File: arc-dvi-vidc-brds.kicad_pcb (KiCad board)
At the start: 4 copper layers, 75.8 x 90.5 mm, 32 parts, among them IC1 SN74ALVC164245, IC2 SN74ALVC164245, IC3 SN74ALVC164245, J1 Connector_50pin_FFC, U1 MIC5219 3.3V

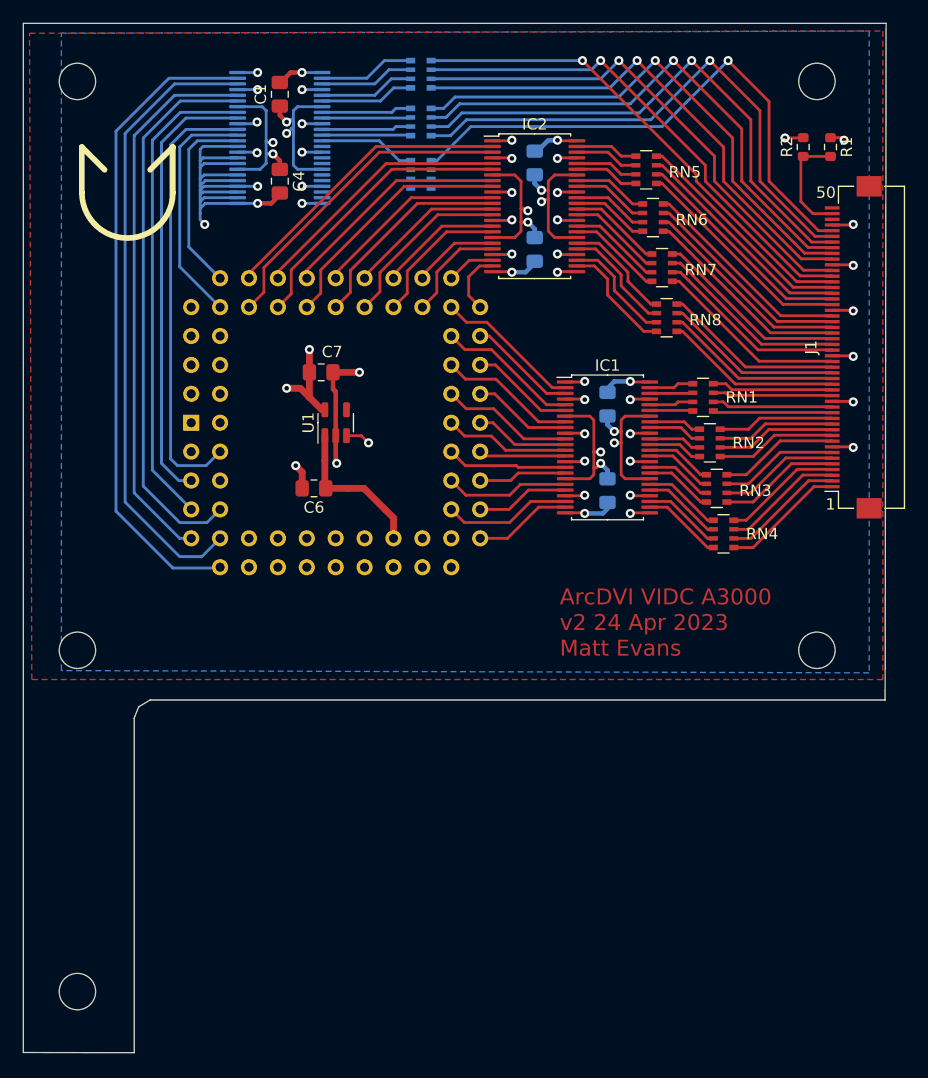
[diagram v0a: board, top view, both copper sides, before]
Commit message: Tweaks to cap positions, power planes
In good shape now, a few minor tweaks to go
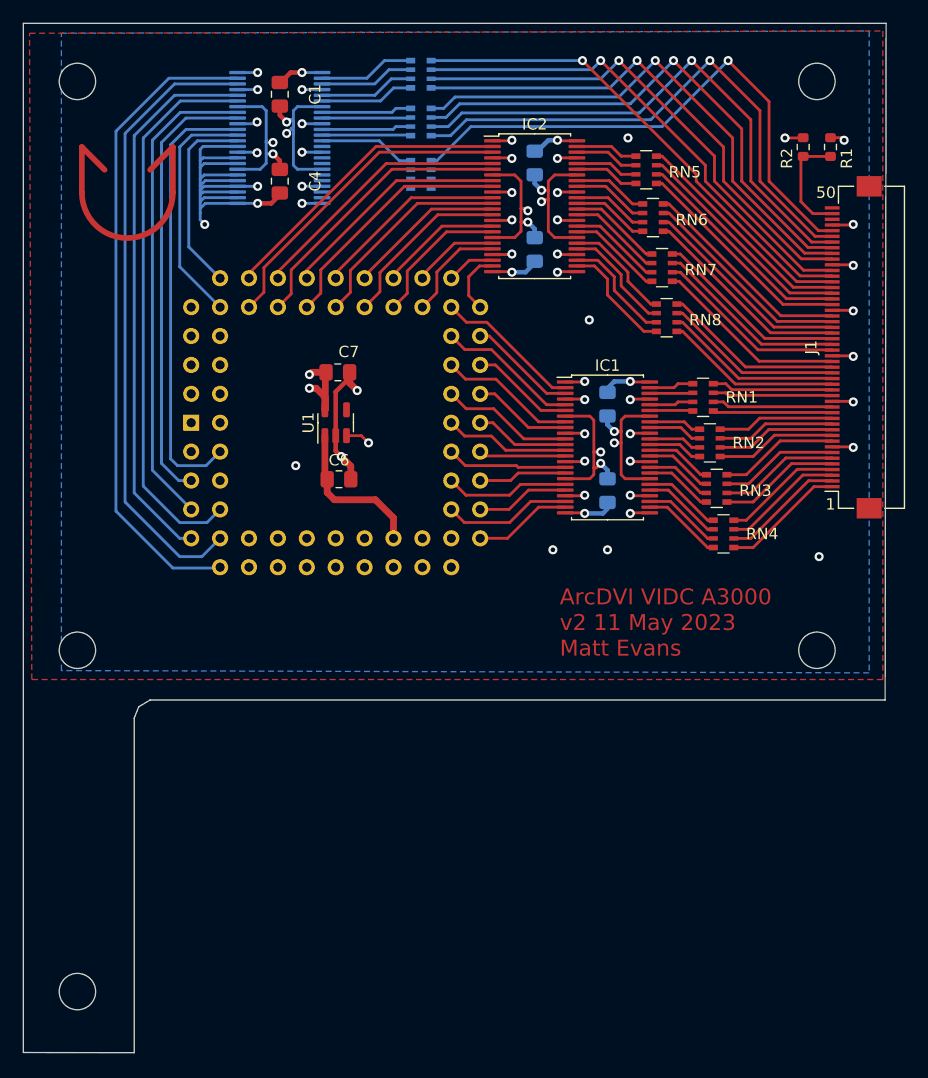
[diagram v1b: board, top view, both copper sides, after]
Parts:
- moved C6 2.34 mm to (83.0, 105.0), turned to 0 degrees
- moved C7 1.46 mm to (82.9, 95.6)
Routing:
- net +3V3: track 242.3 -> 240.2 mm
- net GND: track 413.6 -> 413.3 mm, vias 47 -> 52
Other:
- board text added: "ArcDVI VIDC A3000 v2 11 May 2023 Matt Evans"
- board text removed: "ArcDVI VIDC A3000 v2 24 Apr 2023 Matt Evans"

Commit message: Add logo
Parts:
- added G***: LOGO, LOGO, F.Cu at (94.5, 71.7)

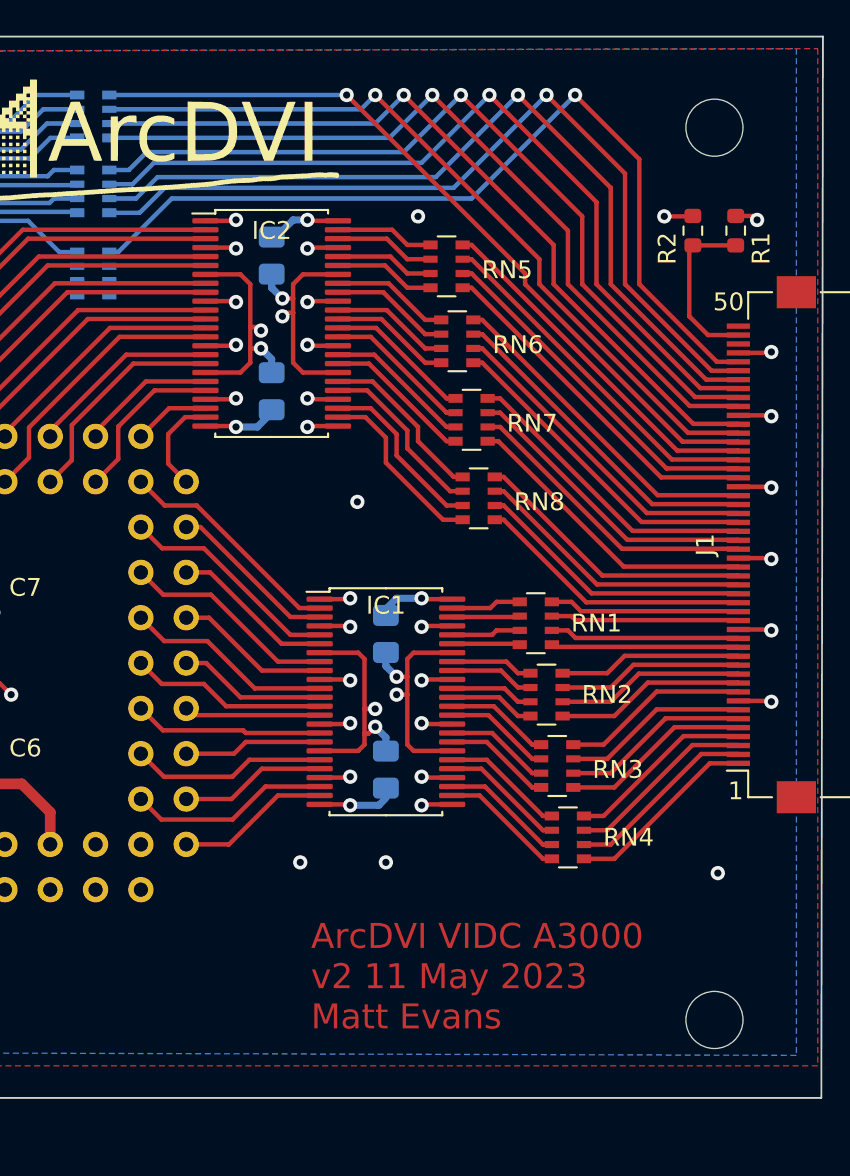
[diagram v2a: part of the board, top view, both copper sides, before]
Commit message: Moved holes to 60mm centers
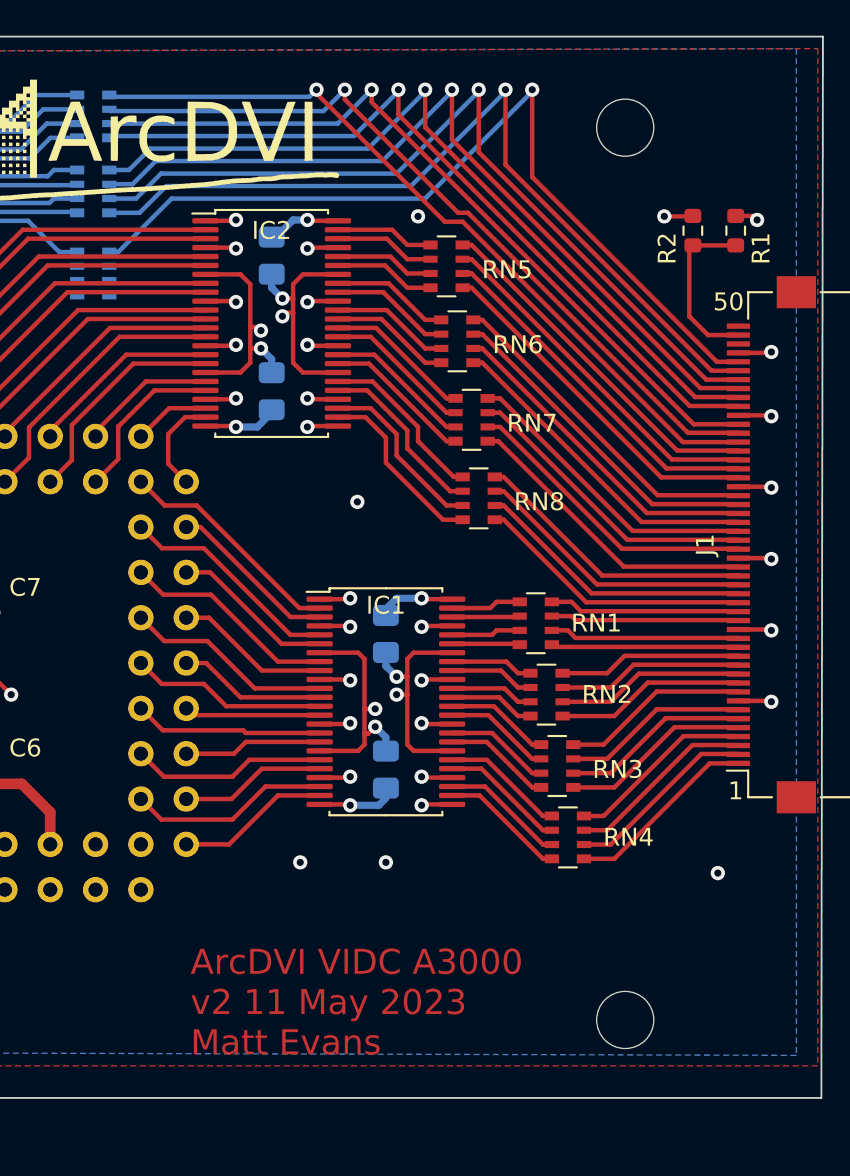
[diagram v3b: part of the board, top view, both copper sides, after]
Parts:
- moved REF** 5.00 mm to (120.0, 120.0)
- moved REF** 5.00 mm to (120.0, 70.0)
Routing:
- net Net-(J1-Pad46): track 49.2 -> 48.3 mm
- net Net-(J1-Pad45): track 48.0 -> 47.2 mm
- net Net-(J1-Pad44): track 47.4 -> 46.6 mm
- net Net-(J1-Pad43): track 46.8 -> 46.1 mm
- net Net-(J1-Pad42): track 46.2 -> 45.5 mm
- net Net-(J1-Pad39): track 44.8 -> 44.2 mm
- net Net-(J1-Pad41): track 45.2 -> 44.6 mm

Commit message: Update date
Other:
- board text added: "ArcDVI VIDC A3000 v2 1 June 2023 Matt Evans"
- board text removed: "ArcDVI VIDC A3000 v2 11 May 2023 Matt Evans"
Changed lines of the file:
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@@
       (xy 131.08 64.895)
     ) (layer "Edge.Cuts") (width 0.1) (fill none))
-  (gr_text "ArcDVI VIDC A3000\nv2 11 May 2023\nMatt Evans" (at 95.64 119.02) (layer "F.Cu")
+  (gr_text "ArcDVI VIDC A3000\nv2 1 June 2023\nMatt Evans" (at 95.64 119.02) (layer "F.Cu")
     (effects (font (size 1.4 1.4) (thickness 0.25)) (justify left))
   )

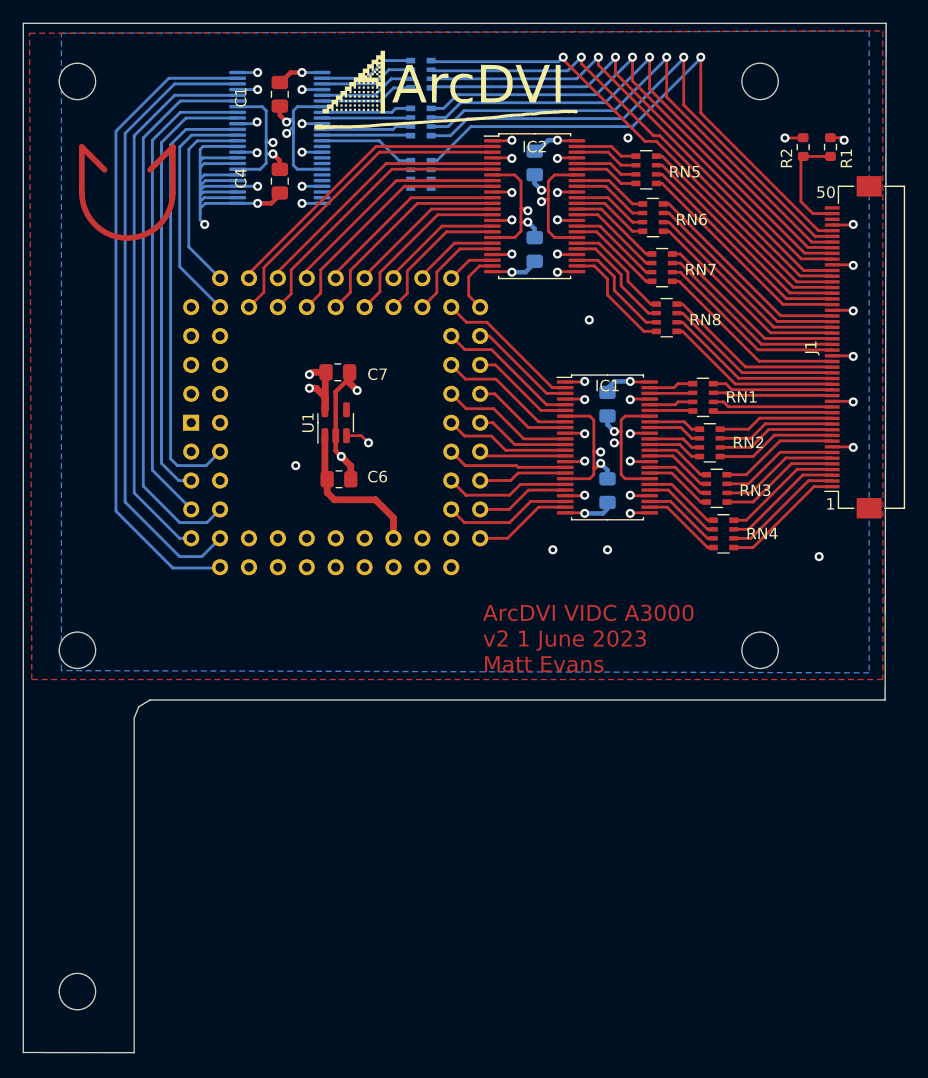
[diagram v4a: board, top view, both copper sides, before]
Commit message: Move regulator, move holes
Reg move now makes PLCC socket centre bare, ideal for mechanical pressure point.
Holes now mean main ArcDVI board lines up preciselyish.
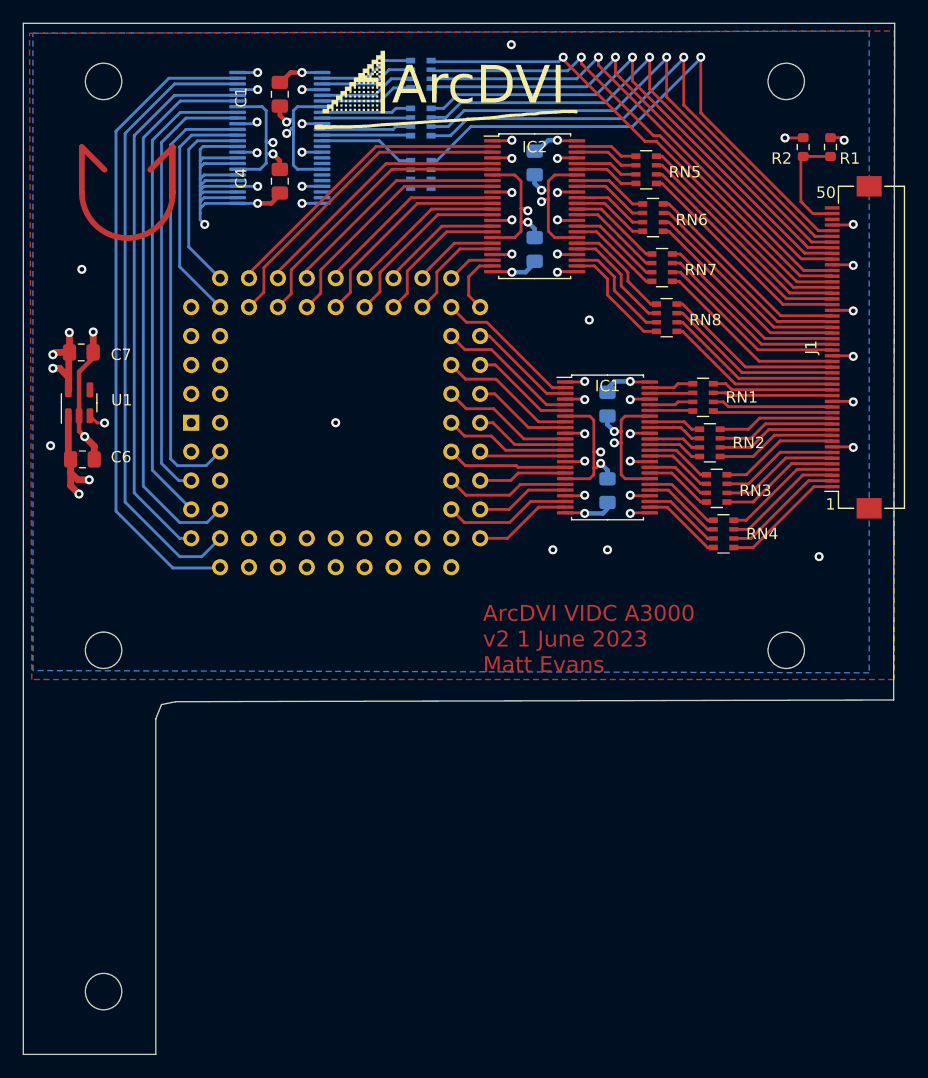
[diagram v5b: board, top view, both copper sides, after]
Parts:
- moved U1 22.6 mm to (60.1, 98.2)
- moved C6 22.6 mm to (60.4, 103.2)
- moved C7 22.6 mm to (60.3, 93.8)
- moved REF** 2.30 mm to (122.3, 120.0)
- moved REF** 2.30 mm to (62.3, 150.0)
- moved REF** 2.30 mm to (122.3, 70.0)
- moved REF** 2.30 mm to (62.3, 120.0)
- moved REF** 2.30 mm to (62.3, 70.0)
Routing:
- net +3V3: track 240.2 -> 179.7 mm, vias 9 -> 10
- net +5V: track 170.7 -> 208.7 mm, vias 7 -> 9
- net GND: track 413.3 -> 408.2 mm, vias 52 -> 54
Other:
- board size 75.8 x 90.5 mm -> 76.6 x 90.6 mm
- board text added: "From TR hole, 20.4 across, 30 down"

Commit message: Add README, licence
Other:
- board text added: "Copyright 2023 Matt Evans CC BY-NC-SA 3.0"
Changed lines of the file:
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@@
     (effects (font (size 1 1) (thickness 0.15)))
+  )
+  (gr_text "Copyright 2023 Matt Evans\n\nCC BY-NC-SA 3.0\n" (at 178.89 170.52) (layer "Cmts.User")
+    (effects (font (size 1 1) (thickness 0.15)) (justify left))
   )
   (gr_text "Machine measurements:\n -- in mm, origin at PLCC centre, where reset sw = north (NOT PCB north)\n\nTop posts dia: 10.5\nBottom posts dia: 12 (say 12 all over)\n- holes 14mm\n\nBorders:\nLK27/bottom border south:  26\nReset sw/top border north: 37\nLeft posts hole to edge, west: 29\n- To centre: 36\nRight post hole to edge, east: 51\n- To centre: 58\nBottom posts centre south: 29\nTop posts centre north: 41\n" (at 19.685 28.575) (layer "Cmts.User")
